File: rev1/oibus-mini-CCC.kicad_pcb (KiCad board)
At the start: 2 copper layers, 37 x 60 mm, 52 parts, among them IC1 LDO40LPU33RY, J1 172310-1202, J3 S5B-ZR-SM4A-TF, J5 uavcan, P1 TC2030-MCP, SW1 SW_Push, U1 NINA-B311-00B, U2 SAM-M8Q, U3 SHT31-DIS-B, U5 DS28E05, U6 TCAN330, U7 STM32F303CCTx, Y1 16M

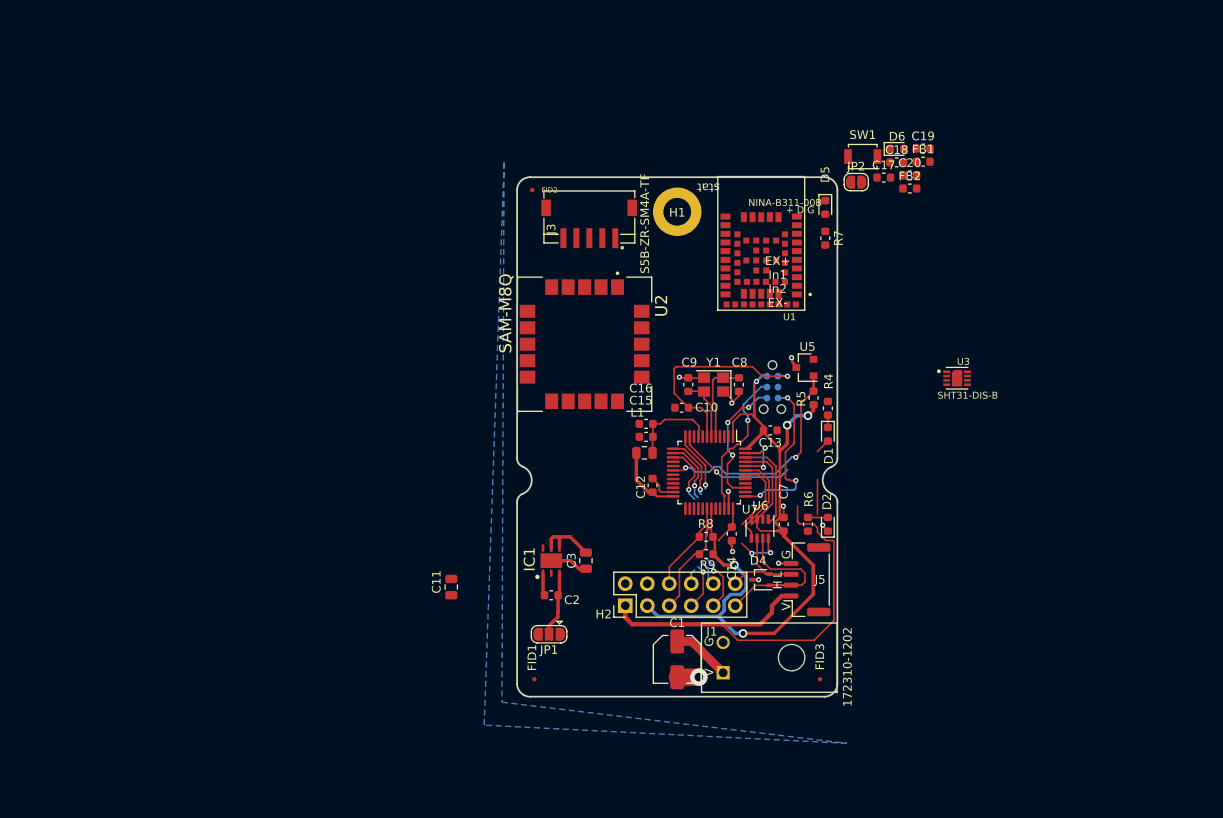
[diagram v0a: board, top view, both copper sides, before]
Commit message: defined power budget and DC-DC converters components; added to schematics incl. footprints
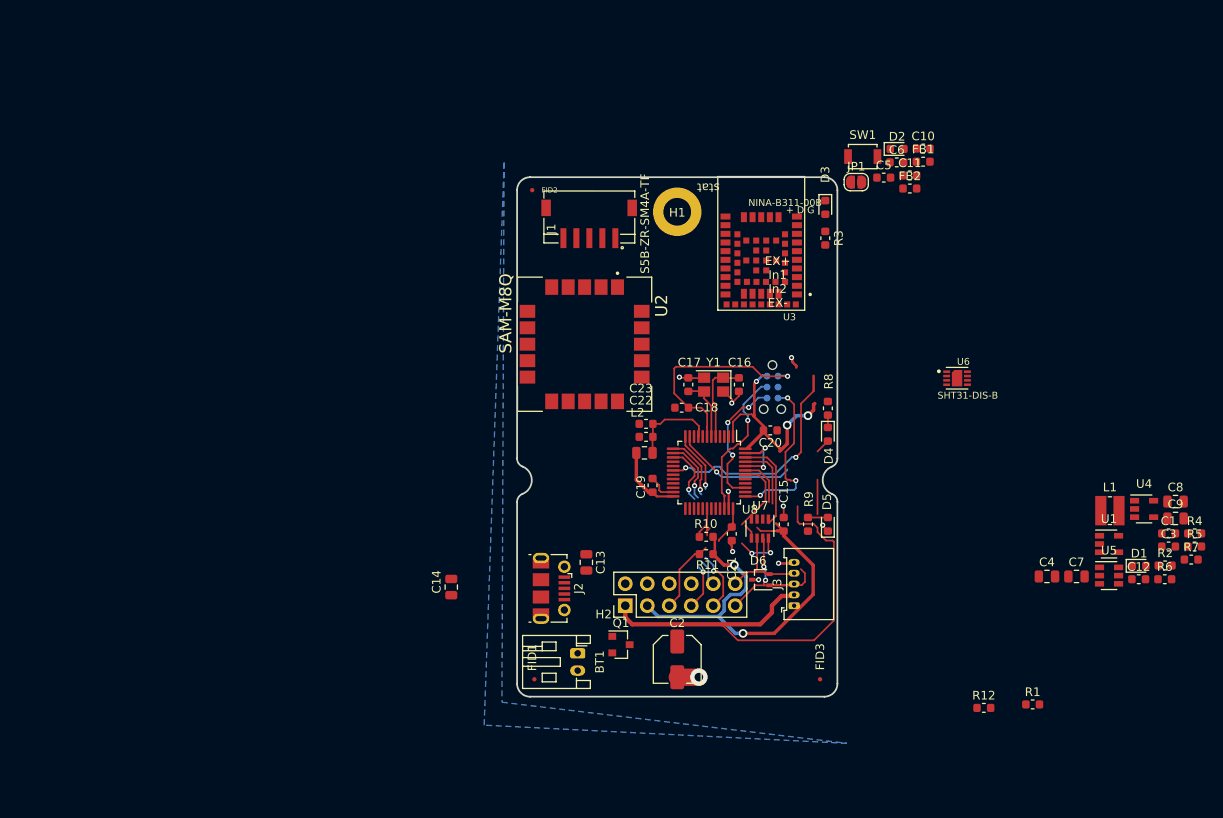
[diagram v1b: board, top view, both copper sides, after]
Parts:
- removed the C2 at (3.95, -11.7)
- removed IC1: LDO40LPU33RY, LDO40LPURY:SON95P300X300X90-7N-D
- removed the J1 at (23.8, -4.50)
- removed J5: uavcan, lib_fp_global:uavcan_connector
- removed the JP1 at (3.70, -7.20)
- added BT1: Battery_Cell, Connector_JST:JST_PH_S2B-PH-K_1x02_P2.00mm_Horizontal, F.Cu at (7.00, -5.00)
- added C1: 1u, Capacitor_SMD:C_0603_1608Metric, F.Cu at (75.3, -18.8)
- added C12: 10n, Capacitor_SMD:C_0603_1608Metric, F.Cu at (71.8, -13.6)
- added C13: 10u, Capacitor_SMD:C_0805_2012Metric, F.Cu at (8.00, -15.5)
- added C4: 4u7, Capacitor_SMD:C_0805_2012Metric, F.Cu at (61.2, -13.9)
- added C7: 4u7, Capacitor_SMD:C_0805_2012Metric, F.Cu at (64.6, -13.9)
- added C8: 4u7, Capacitor_SMD:C_0805_2012Metric, F.Cu at (76.1, -22.5)
- added C9: 10u, Capacitor_SMD:C_0805_2012Metric, F.Cu at (76.1, -20.6)
- added D1: MBR120, Diode_SMD:D_0603_1608Metric, F.Cu at (71.8, -15.1)
- added J2: USB_B_Micro, Connector_USB:USB_Micro-B_Molex-105017-0001, F.Cu at (4.00, -12.5)
- added J3: uavcan_5pins, lib_fp_global:Molex_PicoBlade_53048-0510_1x05_P1.25mm_Horizontal, F.Cu at (32.0, -10.5)
- added L1: 4u7, Inductor_SMD:L_Wuerth_MAPI-3010, F.Cu at (68.5, -21.5)
- added Q1: DMG3415U-7, Package_TO_SOT_SMD:SOT-23, F.Cu at (12.0, -6.00)
- added R1: 100k, Resistor_SMD:R_0603_1608Metric, F.Cu at (59.6, 0.91)
- added R12: 4.7k, Resistor_SMD:R_0603_1608Metric, F.Cu at (53.9, 1.31)
- added R2: 2k, Resistor_SMD:R_0603_1608Metric, F.Cu at (74.9, -15.1)
- added R4: 309k, Resistor_SMD:R_0603_1608Metric, F.Cu at (78.3, -18.8)
- added R6: 100k, Resistor_SMD:R_0603_1608Metric, F.Cu at (74.8, -13.6)
- added R7: 309k, Resistor_SMD:R_0603_1608Metric, F.Cu at (77.9, -15.8)
- added U1: AP2112K-3.3, Package_TO_SOT_SMD:SOT-23-5, F.Cu at (68.4, -17.6)
- added U4: MCP73831-2-OT, Package_TO_SOT_SMD:SOT-23-5, F.Cu at (72.4, -21.7)
- C3: value 4.7u -> 1u; footprint Capacitor_SMD:C_0805_2012Metric -> Capacitor_SMD:C_0603_1608Metric
- R3: renamed from R7; value 330R -> 430R
- R5: value 4.7k -> 976k
- U5: value DS28E05 -> MCP1624T; footprint Package_TO_SOT_SMD:SOT-23 -> Package_TO_SOT_SMD:SOT-23-6
- moved C3 67.3 mm to (75.3, -17.3), turned to 0 degrees
- moved R5 47.2 mm to (78.3, -17.3), turned to 0 degrees
- moved U5 42.6 mm to (68.4, -14.0), turned to 0 degrees
- renumbered C19 to C10, C20 to C11, C11 to C14, C7 to C15, C8 to C16, C9 to C17, C10 to C18, C12 to C19, C1 to C2, C13 to C20, C14 to C21, C15 to C22, C16 to C23, C17 to C5, C18 to C6, D6 to D2, D5 to D3, D1 to D4, D2 to D5, D4 to D6, J3 to J1, JP2 to JP1, L1 to L2, R8 to R10, R9 to R11, R4 to R8, R6 to R9, U1 to U3, U3 to U6, U6 to U7, U7 to U8
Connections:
- C2 pad 1: VBUS -> /VIN
- D3 pad 1: GND -> Net-(D3-Pad1)
- D4 pad 2: +5V -> +3V3
- R3 pad 1: Net-(R7-Pad1) -> VBUS
- R5 pad 1: +3V3 -> Net-(R4-Pad2)
- R5 pad 2: /EEPROM -> GND
- U5 pad 1: /EEPROM -> Net-(L1-Pad2)
- U5 pad 2: (no net) -> GND
- U5 pad 3: GND -> (no net)
- U8 pad 11: Net-(R7-Pad1) -> (no net)
- U8 pad 18: /EEPROM -> (no net)
- U8 pad 32: (no net) -> /USB_DM
- U8 pad 33: (no net) -> /USB_DP
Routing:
- net (no net): track 0.00 -> 40.4 mm, vias 0 -> 3
- net /EEPROM: track 26.2 -> 0.00 mm, vias 2 -> 0
- net +3V3: track 104.6 -> 89.8 mm
- net Net-(R7-Pad1): track 14.2 -> 0.00 mm, vias 1 -> 0
- net Net-(C2-Pad1): track 7.55 -> 0.00 mm
- net GND: track 38.4 -> 31.4 mm
- net /SCL: track 11.8 -> 4.79 mm
- net VBUS: track 6.80 -> 0.00 mm
- net /SDA: track 14.7 -> 9.50 mm
- net /CAN_SHDN: track 11.3 -> 7.45 mm
- net /CAN_RX: track 11.0 -> 7.58 mm
- net CAN_H: track 20.4 -> 18.6 mm, vias 0 -> 2
- net /P4: track 8.77 -> 7.03 mm
- net +5V: track 59.4 -> 57.7 mm

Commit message: finished all pin assignments. pushed to layout
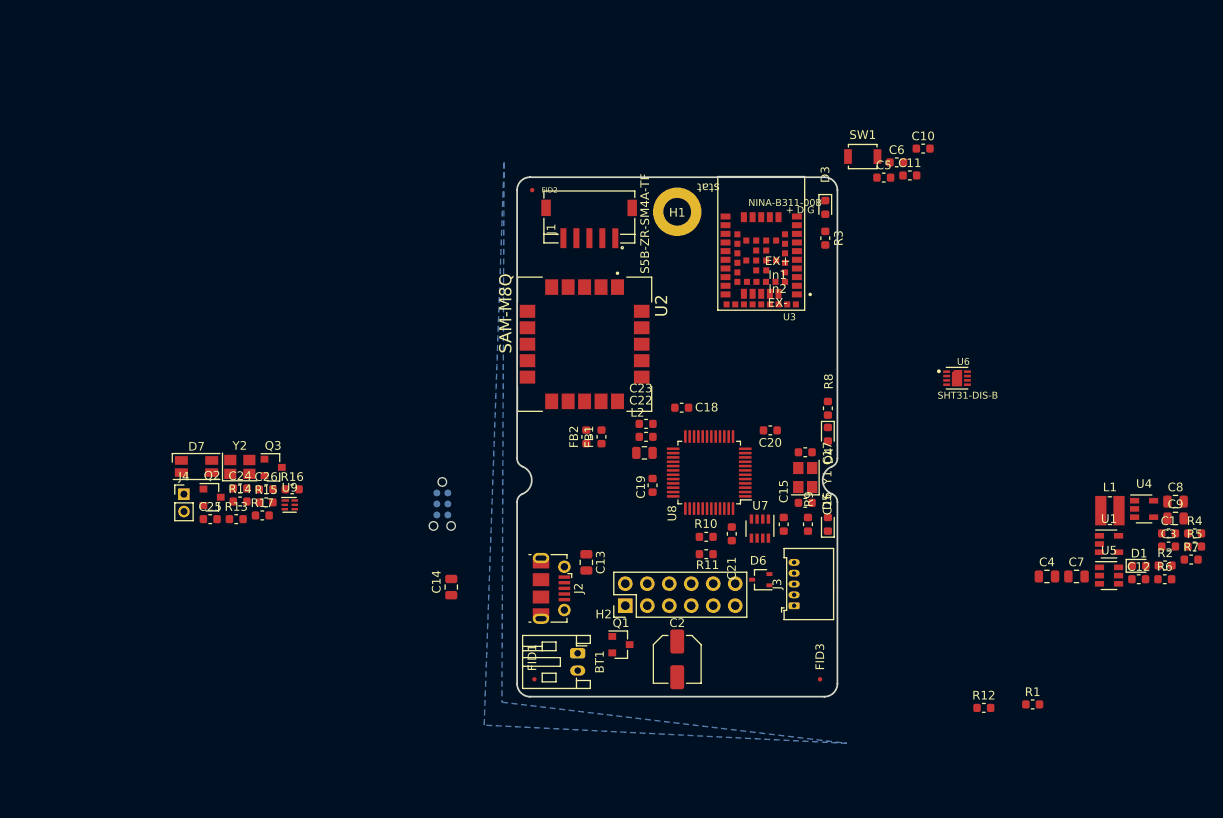
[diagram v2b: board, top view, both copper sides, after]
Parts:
- removed D2: D, Diode_SMD:D_0603_1608Metric
- removed JP1: SolderJumper_2_Open, Jumper:SolderJumper-2_P1.3mm_Open_RoundedPad1.0x1.5mm
- added C24: 1u, Capacitor_SMD:C_0603_1608Metric, F.Cu at (-32.0, -24.0)
- added C25: 10p, Capacitor_SMD:C_0603_1608Metric, F.Cu at (-35.4, -20.5)
- added C26: 10p, Capacitor_SMD:C_0603_1608Metric, F.Cu at (-29.0, -23.9)
- added D7: LED_ABRG, LED_SMD:LED_RGB_1210, F.Cu at (-37.0, -26.6)
- added J4: Conn_01x02_Female, Connector_PinHeader_2.00mm:PinHeader_1x02_P2.00mm_Vertical, F.Cu at (-38.5, -23.4)
- added Q2: DMG3415U-7, Package_TO_SOT_SMD:SOT-23, F.Cu at (-35.2, -23.0)
- added Q3: DMG3415U-7, Package_TO_SOT_SMD:SOT-23, F.Cu at (-28.2, -26.5)
- added R13: 430R, Resistor_SMD:R_0603_1608Metric, F.Cu at (-32.4, -20.5)
- added R14: 1k, Resistor_SMD:R_0603_1608Metric, F.Cu at (-32.0, -22.5)
- added R15: 1k, Resistor_SMD:R_0603_1608Metric, F.Cu at (-29.0, -22.4)
- added R16: 1k, Resistor_SMD:R_0603_1608Metric, F.Cu at (-26.0, -23.9)
- added R17: 2k7, Resistor_SMD:R_0603_1608Metric, F.Cu at (-29.4, -20.9)
- added U9: DW01C-G, Package_SON:WSON-6_1.5x1.5mm_P0.5mm, F.Cu at (-26.3, -22.1)
- added Y2: 32kHz, Crystal:Crystal_SMD_SeikoEpson_FA238-4Pin_3.2x2.5mm, F.Cu at (-32.0, -26.5)
- moved FB1 48.9 mm to (9.75, -30.0), turned to 90 degrees
- moved FB2 47.1 mm to (8.00, -30.0), turned to 90 degrees
- moved P1 40.5 mm to (-8.63, -22.2)
- moved C16 15.7 mm to (33.3, -22.4), turned to 180 degrees
- moved C17 15.6 mm to (33.3, -28.2), turned to 180 degrees
- moved Y1 15.1 mm to (33.3, -25.3), turned to 90 degrees
- turned U8 to 180 degrees
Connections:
- net CAN_H renamed /CAN_H
- net CAN_L renamed /CAN_L
- BT1 pad 2: GND -> Net-(BT1-Pad2)
- C13 pad 1: Net-(C13-Pad1) -> GND
- FB1 pad 1: (no net) -> GPS_RX
- FB2 pad 1: (no net) -> GPS_TX
- H2 pad 10: /P2 -> /~SPI_ADS_CS
- H2 pad 7: /P3 -> /SPI_MOSI
- H2 pad 8: /P4 -> /SPI_MISO
- H2 pad 9: /P1 -> /SPI_SCK
- J1 pad 2: (no net) -> /SPS_RX
- J1 pad 3: (no net) -> /SPS_TX
- J2 pad 5: Net-(C13-Pad1) -> GND
- J2 pad 6: Net-(C13-Pad1) -> GND
- R10 pad 2: /SCL -> /SDA
- R11 pad 2: /SDA -> /SCL
- U2 pad 1: Net-(U2-Pad1) -> GND
- U2 pad 10: Net-(U2-Pad1) -> GND
- U2 pad 11: Net-(U2-Pad1) -> GND
- U2 pad 15: Net-(U2-Pad1) -> GND
- U2 pad 16: Net-(U2-Pad1) -> GND
- U2 pad 20: Net-(U2-Pad1) -> GND
- U2 pad 3: Net-(D2-Pad1) -> +3V3
- U2 pad 4: Net-(U2-Pad1) -> GND
- U2 pad 5: Net-(U2-Pad1) -> GND
- U2 pad 6: Net-(U2-Pad1) -> GND
- U2 pad 7: Net-(JP1-Pad1) -> /GPS_TIME
- U3 pad 1: (no net) -> /RED
- U3 pad 16: (no net) -> NINA_DTR
- U3 pad 17: (no net) -> NINA_DSR
- U3 pad 20: (no net) -> NINA_RTS
- U3 pad 21: (no net) -> NINA_CTS
- U3 pad 22: (no net) -> NINA_TX
- U3 pad 23: (no net) -> NINA_RX
- U3 pad 28: (no net) -> Net-(J4-Pad2)
- U3 pad 29: (no net) -> Net-(J4-Pad1)
- U3 pad 7: (no net) -> /GREEN
- U3 pad 8: (no net) -> /BLUE
- U5 pad 3: (no net) -> /5V_EN
- U6 pad 3: (no net) -> /SHT_ALERT
- U8 pad 10: (no net) -> NINA_RTS
- U8 pad 11: (no net) -> NINA_CTS
- U8 pad 12: /P1 -> NINA_RX
- U8 pad 13: /P2 -> NINA_TX
- U8 pad 14: /P3 -> NINA_DTR
- U8 pad 15: /P4 -> NINA_DSR
- U8 pad 17: (no net) -> /BAT_MEAS
- U8 pad 18: (no net) -> /CAN_SILENT
- U8 pad 19: (no net) -> /CAN_SHDN
- U8 pad 20: (no net) -> /GPS_TIME
- U8 pad 21: (no net) -> /SPS_RX
- U8 pad 22: (no net) -> /SPS_TX
- U8 pad 25: (no net) -> /~SPI_ADS_CS
- U8 pad 26: (no net) -> /SPI_SCK
- U8 pad 27: (no net) -> /SPI_MISO
- U8 pad 28: (no net) -> /SPI_MOSI
- U8 pad 3: (no net) -> Net-(C25-Pad1)
- U8 pad 30: /SCL -> GPS_RX
- U8 pad 31: /SDA -> GPS_TX
- U8 pad 38: (no net) -> /5V_EN
- U8 pad 4: (no net) -> Net-(C26-Pad2)
- U8 pad 41: (no net) -> /SHT_ALERT
- U8 pad 42: /CAN_SILENT -> /SCL
- U8 pad 43: /CAN_SHDN -> /SDA
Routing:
- net +3V3: track 89.8 -> 0.00 mm, vias 5 -> 0
- net +5V: track 57.7 -> 0.00 mm
- net (no net): track 40.4 -> 0.00 mm, vias 3 -> 0
- net GND: track 31.4 -> 0.00 mm, vias 12 -> 0
- net /~RESET: track 25.0 -> 0.00 mm, vias 1 -> 0
- net /SWDCLK: track 19.6 -> 0.00 mm, vias 3 -> 0
- net /CAN_H: track 18.6 -> 0.00 mm, vias 2 -> 0
- net /SWDIO: track 17.4 -> 0.00 mm, vias 1 -> 0
- net /SWDSWO: track 15.4 -> 0.00 mm, vias 3 -> 0
- net /CAN_SILENT: track 14.4 -> 0.00 mm, vias 2 -> 0
- net /P1: track 14.1 -> 0.00 mm, vias 2 -> 0
- net /P3: track 12.7 -> 0.00 mm, vias 2 -> 0
- net /CAN_L: track 11.5 -> 0.00 mm
- net /CAN_TX: track 11.1 -> 0.00 mm
- net /P2: track 10.6 -> 0.00 mm, vias 1 -> 0
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
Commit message: grove connector and boot pin correction. added Licence file
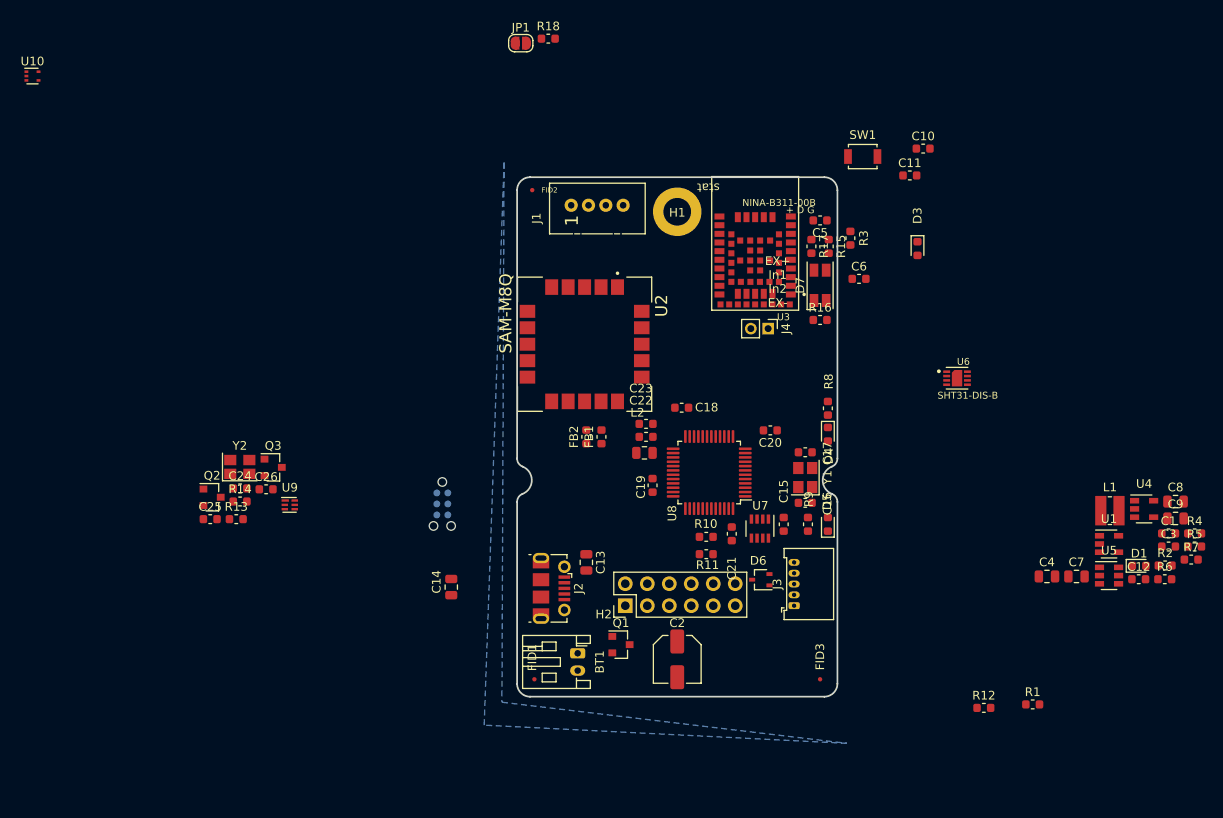
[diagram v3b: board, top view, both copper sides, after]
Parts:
- added JP1: Jumper_NO_Small, Jumper:SolderJumper-2_P1.3mm_Open_RoundedPad1.0x1.5mm, F.Cu at (0.43, -75.5)
- added R18: 4.7k, Resistor_SMD:R_0603_1608Metric, F.Cu at (3.61, -76.0)
- added U10: TPD3E001DRLR, Package_TO_SOT_SMD:SOT-553, F.Cu at (-56.0, -71.7)
- J1: value S5B-ZR-SM4A-TF -> Conn_01x04_Female; footprint lib_fp:JST_S5B-ZR-SM4A-TF -> lib_fp:Grove_1x04
- moved D7 75.0 mm to (35.0, -47.5), turned to 90 degrees
- moved R15 71.4 mm to (36.0, -52.0), turned to 270 degrees
- moved R17 70.6 mm to (34.0, -52.0), turned to 270 degrees
- moved J4 70.1 mm to (29.0, -42.5), turned to 270 degrees
- moved R16 64.0 mm to (35.0, -43.5)
- moved C6 14.1 mm to (39.5, -48.2)
- moved D3 11.7 mm to (46.2, -51.8)
- moved C5 8.86 mm to (35.0, -55.0), turned to 180 degrees
- moved J1 4.75 mm to (6.25, -56.8), turned to 90 degrees
- moved R3 2.90 mm to (38.5, -53.0)
- moved U3 0.70 mm to (27.5, -50.5)
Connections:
- C18 pad 1: GND -> /~RESET
- C18 pad 2: /~RESET -> GND
- J1 pad 1: +5V -> /SPS_RX
- J1 pad 2: /SPS_RX -> /SPS_TX
- J1 pad 3: /SPS_TX -> +5V
- J1 pad 4: (no net) -> GND
- J2 pad 4: (no net) -> /ID
- U8 pad 44: GND -> /BOOT

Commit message: finished component placement
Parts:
- removed C13: 10u, Capacitor_SMD:C_0805_2012Metric
- removed C6: 100n, Capacitor_SMD:C_0603_1608Metric
- J4: footprint Connector_PinHeader_2.00mm:PinHeader_1x02_P2.00mm_Vertical -> Jumper:SolderJumper-2_P1.3mm_Open_RoundedPad1.0x1.5mm; moved to B.Cu
- P1: moved to F.Cu
- moved U10 87.1 mm to (8.00, -12.5)
- moved C25 70.9 mm to (35.0, -28.5), turned to 180 degrees
- moved Y2 67.2 mm to (35.0, -31.5), turned to 90 degrees
- moved R5 65.6 mm to (12.8, -21.6), turned to 90 degrees
- moved R4 65.5 mm to (12.8, -18.1), turned to 90 degrees
- moved C26 64.8 mm to (35.0, -34.5), turned to 180 degrees
- moved C9 61.1 mm to (15.1, -16.9), turned to 90 degrees
- moved R2 57.9 mm to (18.0, -4.25)
- moved R7 57.7 mm to (21.8, -2.25), turned to 180 degrees
- moved D3 57.3 mm to (7.50, -9.50), turned to 90 degrees
- moved C8 57.3 mm to (21.0, -6.75), turned to 90 degrees
- moved U4 56.7 mm to (17.8, -6.75), turned to 180 degrees
- moved U5 53.1 mm to (15.8, -21.1), turned to 270 degrees
- moved R3 52.4 mm to (9.25, -9.50)
- moved Q3 52.4 mm to (18.0, -1.75)
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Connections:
- U10 pad 1: /USB_DP -> /USB_DM
- U10 pad 2: /USB_DM -> /USB_DP
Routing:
- net /SWDCLK: track 0.00 -> 33.7 mm, vias 0 -> 2
- net /USB_DP: track 0.00 -> 33.1 mm
- net /USB_DM: track 0.00 -> 32.6 mm
- net /CAN_SHDN: track 0.00 -> 30.9 mm, vias 0 -> 2
- net /SWDSWO: track 0.00 -> 29.4 mm, vias 0 -> 2
- net /BOOT: track 0.00 -> 26.5 mm, vias 0 -> 2
- net /SWDIO: track 0.00 -> 25.8 mm, vias 0 -> 2
- net /5V_EN: track 0.00 -> 23.5 mm
- net /CAN_TX: track 0.00 -> 13.9 mm
- net /CAN_RX: track 0.00 -> 13.3 mm
- net GPS_TX: track 0.00 -> 12.9 mm
- net GPS_RX: track 0.00 -> 12.4 mm
- net Net-(C16-Pad1): track 0.00 -> 10.9 mm
- net NINA_DTR: track 0.00 -> 10.2 mm
- net NINA_RTS: track 0.00 -> 9.24 mm
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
